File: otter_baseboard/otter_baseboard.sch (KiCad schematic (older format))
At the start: 25 parts, among them J1 Conn_02x20_Odd_Even, J2 Conn_02x08_Odd_Even, J3 Conn_02x08_Odd_Even, J4 Conn_02x08_Odd_Even, J5 Conn_02x08_Odd_Even, J6 Conn_02x08_Odd_Even, J7 Conn_02x20_Odd_Even

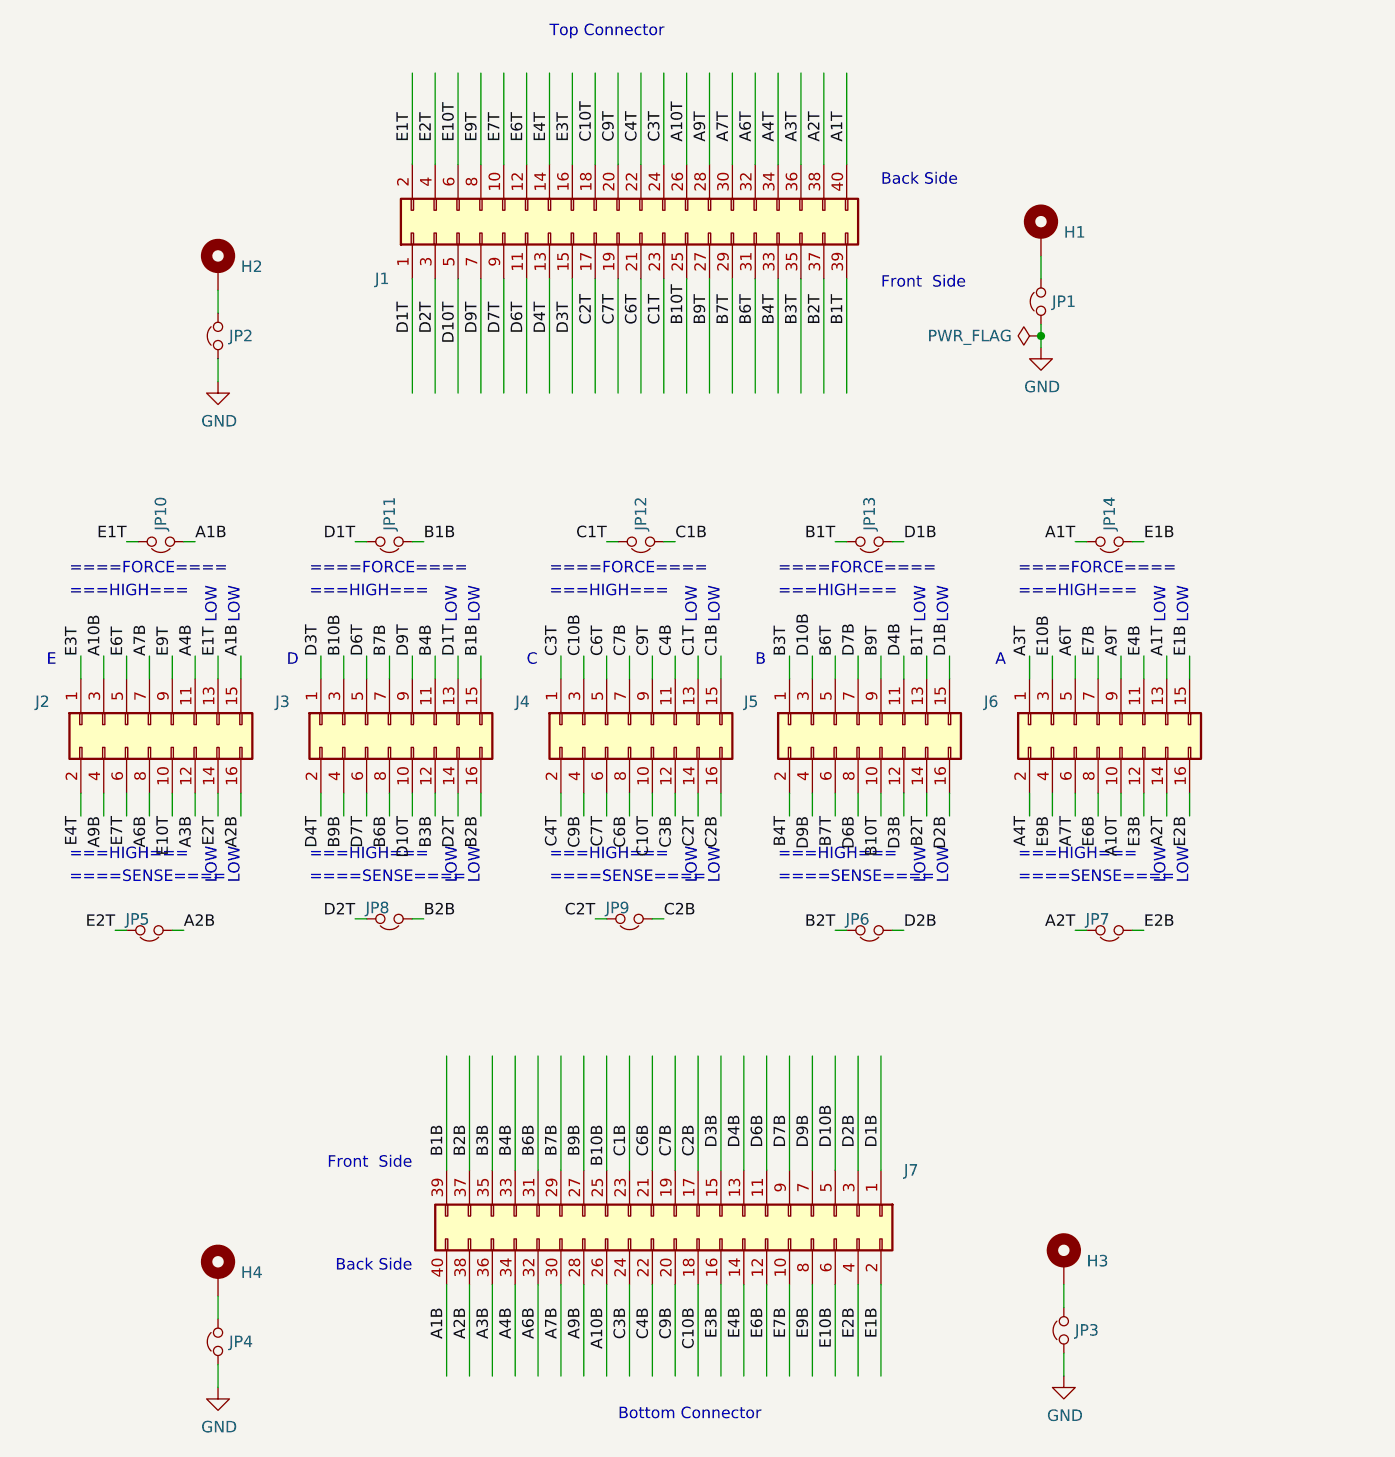
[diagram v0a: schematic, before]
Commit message: baseboard routed
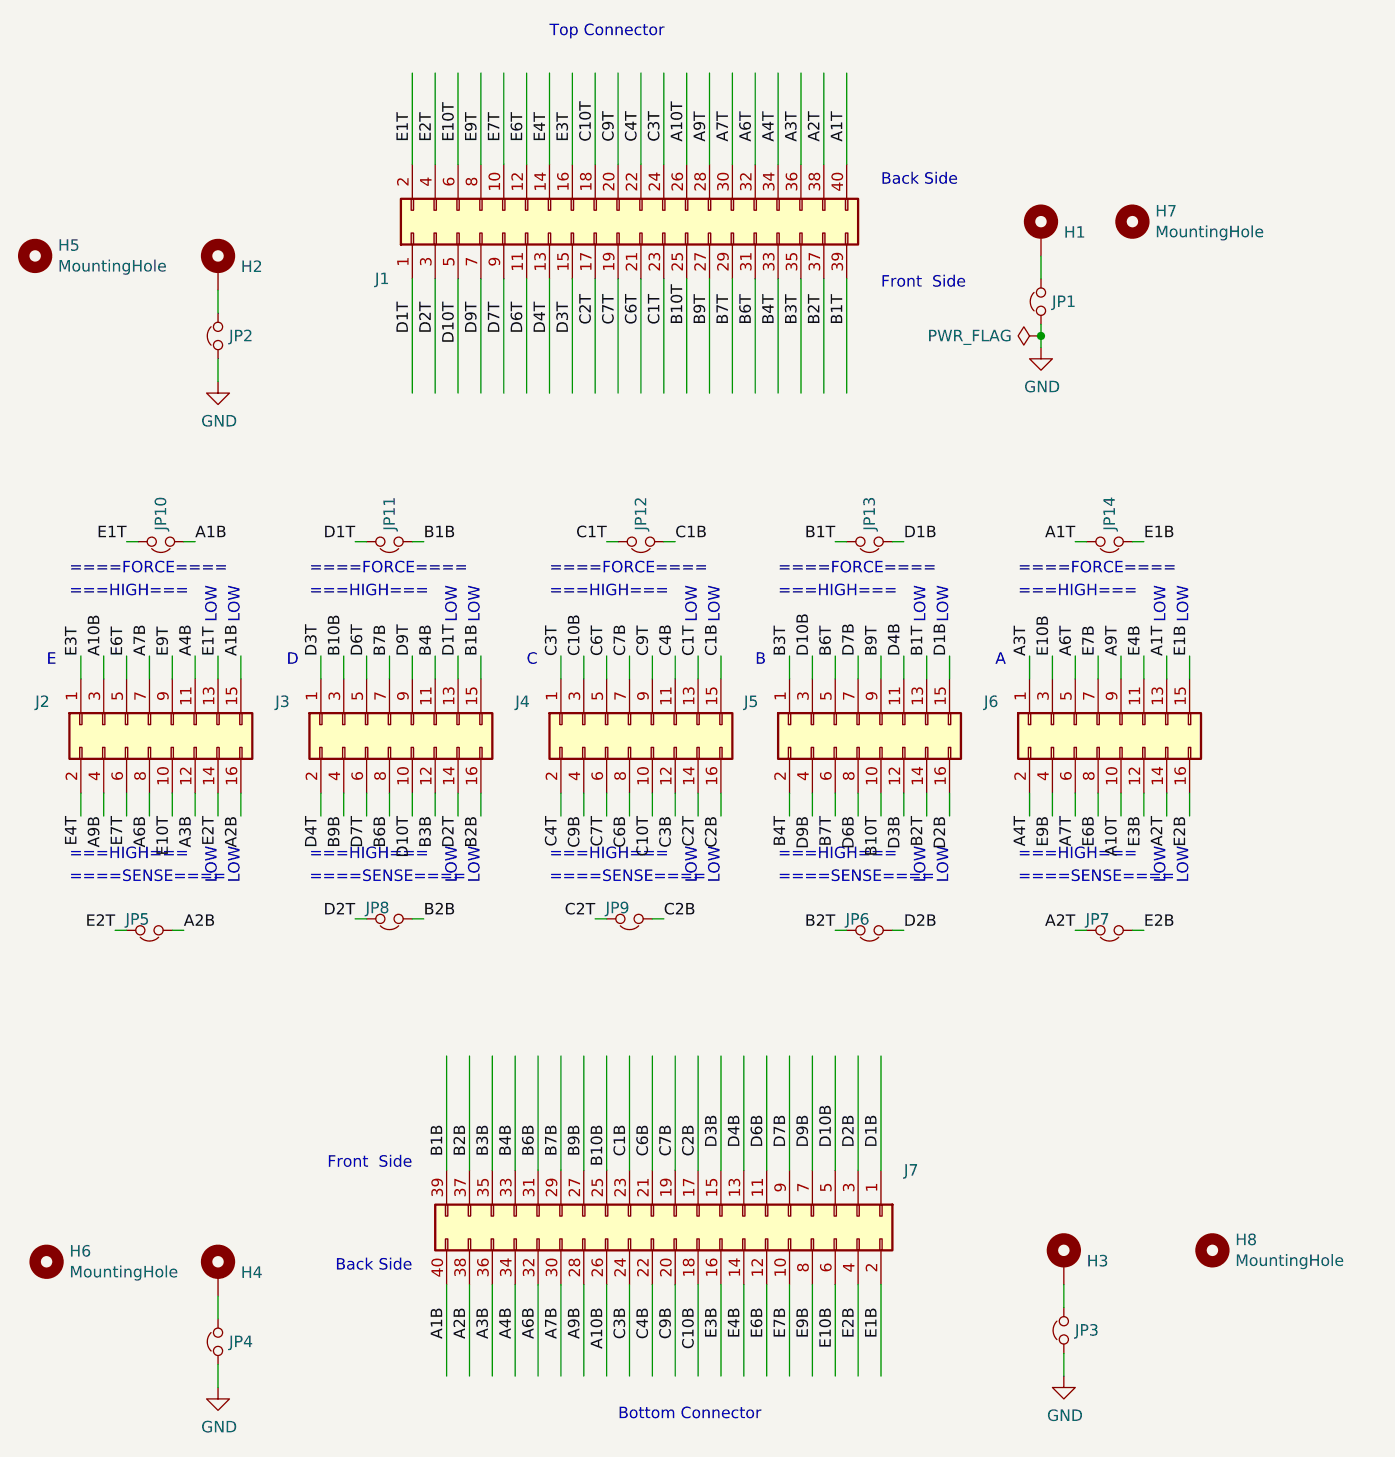
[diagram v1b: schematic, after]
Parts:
- added H5, H6, H7, H8: MountingHole, MountingHole:MountingHole_4.3mm_M4_ISO7380, symbol Mechanical:MountingHole
- J1, J7: footprint Connector_PCBEdge:Samtec_MECF-20-01-NP-L-DV-WT_2x20_P1.27mm_Socket_Horizontal -> custom_footprints:Samtec_MECF-20-01-NP-L-DV-WT_2x20_P1.27mm_Socket_Horizontal_mod
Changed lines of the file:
@@
 F 0 "J1" V 6750 4350 50  0000 L CNN
 F 1 "Conn_02x20_Odd_Even" V 6955 4329 50  0001 L CNN
-F 2 "Connector_PCBEdge:Samtec_MECF-20-01-NP-L-DV-WT_2x20_P1.27mm_Socket_Horizontal" H 6950 3350 50  0001 C CNN
+F 2 "custom_footprints:Samtec_MECF-20-01-NP-L-DV-WT_2x20_P1.27mm_Socket_Horizontal_mod" H 6950 3350 50  0001 C CNN
 F 3 "~" H 6950 3350 50  0001 C CNN
 F 4 "samtec" H 6950 3350 50  0001 C CNN "mfg"
@@
 F 0 "J7" V 7000 8650 50  0000 L CNN
 F 1 "Conn_02x20_Odd_Even" V 7205 8629 50  0001 L CNN
-F 2 "Connector_PCBEdge:Samtec_MECF-20-01-NP-L-DV-WT_2x20_P1.27mm_Socket_Horizontal" H 7200 7650 50  0001 C CNN
+F 2 "custom_footprints:Samtec_MECF-20-01-NP-L-DV-WT_2x20_P1.27mm_Socket_Horizontal_mod" H 7200 7650 50  0001 C CNN
 F 3 "~" H 7200 7650 50  0001 C CNN
 F 4 "samtec" H 7200 7650 50  0001 C CNN "mfg"
@@
 	0    -1   1    0
 $EndComp
+$Comp
+L Mechanical:MountingHole H7
+U 1 1 5E2D2B9E
+P 9200 3300
+F 0 "H7" H 9300 3346 50  0000 L CNN
+F 1 "MountingHole" H 9300 3255 50  0000 L CNN
+F 2 "MountingHole:MountingHole_4.3mm_M4_ISO7380" H 9200 3300 50  0001 C CNN
+F 3 "~" H 9200 3300 50  0001 C CNN
+	1    9200 3300
+	1    0    0    -1
+$EndComp
+$Comp
+L Mechanical:MountingHole H5
+U 1 1 5E2D391D
+P 4400 3450
+F 0 "H5" H 4500 3496 50  0000 L CNN
+F 1 "MountingHole" H 4500 3405 50  0000 L CNN
+F 2 "MountingHole:MountingHole_4.3mm_M4_ISO7380" H 4400 3450 50  0001 C CNN
+F 3 "~" H 4400 3450 50  0001 C CNN
+	1    4400 3450
+	1    0    0    -1
+$EndComp
+$Comp
+L Mechanical:MountingHole H6
+U 1 1 5E2D5387
+P 4450 7850
+F 0 "H6" H 4550 7896 50  0000 L CNN
+F 1 "MountingHole" H 4550 7805 50  0000 L CNN
+F 2 "MountingHole:MountingHole_4.3mm_M4_ISO7380" H 4450 7850 50  0001 C CNN
+F 3 "~" H 4450 7850 50  0001 C CNN
+	1    4450 7850
+	1    0    0    -1
+$EndComp
+$Comp
+L Mechanical:MountingHole H8
+U 1 1 5E2D5A55
+P 9550 7800
+F 0 "H8" H 9650 7846 50  0000 L CNN
+F 1 "MountingHole" H 9650 7755 50  0000 L CNN
+F 2 "MountingHole:MountingHole_4.3mm_M4_ISO7380" H 9550 7800 50  0001 C CNN
+F 3 "~" H 9550 7800 50  0001 C CNN
+	1    9550 7800
+	1    0    0    -1
+$EndComp
 $EndSCHEMATC

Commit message: enbiggen pcb dowel holes
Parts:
- H5, H6, H7, H8: footprint MountingHole:MountingHole_4.3mm_M4_ISO7380 -> MountingHole:MountingHole_6.4mm_M6
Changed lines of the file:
@@
 F 0 "H7" H 9300 3346 50  0000 L CNN
 F 1 "MountingHole" H 9300 3255 50  0000 L CNN
-F 2 "MountingHole:MountingHole_4.3mm_M4_ISO7380" H 9200 3300 50  0001 C CNN
+F 2 "MountingHole:MountingHole_6.4mm_M6" H 9200 3300 50  0001 C CNN
 F 3 "~" H 9200 3300 50  0001 C CNN
 	1    9200 3300
@@
 F 0 "H5" H 4500 3496 50  0000 L CNN
 F 1 "MountingHole" H 4500 3405 50  0000 L CNN
-F 2 "MountingHole:MountingHole_4.3mm_M4_ISO7380" H 4400 3450 50  0001 C CNN
+F 2 "MountingHole:MountingHole_6.4mm_M6" H 4400 3450 50  0001 C CNN
 F 3 "~" H 4400 3450 50  0001 C CNN
 	1    4400 3450
@@
 F 0 "H6" H 4550 7896 50  0000 L CNN
 F 1 "MountingHole" H 4550 7805 50  0000 L CNN
-F 2 "MountingHole:MountingHole_4.3mm_M4_ISO7380" H 4450 7850 50  0001 C CNN
+F 2 "MountingHole:MountingHole_6.4mm_M6" H 4450 7850 50  0001 C CNN
 F 3 "~" H 4450 7850 50  0001 C CNN
 	1    4450 7850
@@
 F 0 "H8" H 9650 7846 50  0000 L CNN
 F 1 "MountingHole" H 9650 7755 50  0000 L CNN
-F 2 "MountingHole:MountingHole_4.3mm_M4_ISO7380" H 9550 7800 50  0001 C CNN
+F 2 "MountingHole:MountingHole_6.4mm_M6" H 9550 7800 50  0001 C CNN
 F 3 "~" H 9550 7800 50  0001 C CNN
 	1    9550 7800
